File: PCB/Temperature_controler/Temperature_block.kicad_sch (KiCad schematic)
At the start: 16 parts, among them J1 PT IN, J2 Thermocouple IN, SW1 SW_DIP_x05, U2 MAX31865xAP, U3 MAX31856

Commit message: PCB progress
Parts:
- removed SW1: SW_DIP_x05, symbol Switch:SW_DIP_x05
- added C36, C37, C40, C41, C42, C43: 100nF, Capacitor_SMD:C_0805_2012Metric_Pad1.18x1.45mm_HandSolder, symbol Device:C
- added C38, C39: 10nF, Capacitor_SMD:C_0805_2012Metric_Pad1.18x1.45mm_HandSolder, symbol Device:C
- added J11, J12, J13, J15: Conn_01x02_Socket, Connector_Wire:SolderWire-1sqmm_1x02_P5.4mm_D1.4mm_OD2.7mm, symbol Connector:Conn_01x02_Socket
- added J4: T2 IN, TerminalBlock_Phoenix:TerminalBlock_Phoenix_MKDS-1,5-2_1x02_P5.00mm_Horizontal, symbol Connector:Screw_Terminal_01x02
- added J5: RTD2 IN, TerminalBlock_Phoenix:TerminalBlock_Phoenix_MKDS-1,5-4_1x04_P5.00mm_Horizontal, symbol Connector:Screw_Terminal_01x04
- added Q1, Q2, Q3, Q4: BS170F, Package_TO_SOT_SMD:SOT-23, symbol Transistor_FET:BS170F
- added R17, R18: 100Ω, Resistor_SMD:R_0805_2012Metric_Pad1.20x1.40mm_HandSolder, symbol Device:R
- added R19: 400Ω, Resistor_SMD:R_0805_2012Metric_Pad1.20x1.40mm_HandSolder, symbol Device:R
- added R25, R26, R27, R28: 10kΩ, Resistor_SMD:R_0805_2012Metric_Pad1.20x1.40mm_HandSolder, symbol Device:R
- added SW1, SW4: SW_DIP_x04, Button_Switch_SMD:SW_DIP_SPSTx04_Slide_Omron_A6H-4101_W6.15mm_P1.27mm, symbol Switch:SW_DIP_x04
- added U6: MAX31856, Package_SO:TSSOP-14_4.4x5mm_P0.65mm, symbol Sensor_Temperature:MAX31856
- added U7: MAX31865xAP, Package_SO:SSOP-20_5.3x7.2mm_P0.65mm, symbol Sensor_Temperature:MAX31865xAP
- C13, C14, C15, C16, C17, C18, C19, C20: footprint (none) -> Capacitor_SMD:C_0805_2012Metric_Pad1.18x1.45mm_HandSolder
- J1: value PT IN -> RTD1 IN
- J2: value Thermocouple IN -> T1 IN; footprint (none) -> TerminalBlock_Phoenix:TerminalBlock_Phoenix_MKDS-1,5-2_1x02_P5.00mm_Horizontal
- R1, R2, R3: footprint (none) -> Resistor_SMD:R_0805_2012Metric_Pad1.20x1.40mm_HandSolder
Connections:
- net +3.3V: now also C36.1, C37.1, C41.1, C42.1, U6.5 (AVDD), U6.8 (DVDD), U7.2 (DVDD), U7.3 (VDD)
- net GND: now also C36.2, C37.2, C38.2, C39.1, C41.2, C42.2, Q1.2 (S), Q2.2 (S), Q3.2 (S), Q4.2 (S), R25.2, R26.2, R27.2, R28.2, SW1.6, SW4.6, U6.1 (AGND), U6.14 (DGND), U7.13 (GND), U7.18 (DGND), U7.19 (GND)
- net SPI1_CLK: now also U6.10 (SCK), U7.15 (SCLK)
- net SPI1_MISO: now also U6.11 (SDO), U7.17 (SDO)
- net SPI1_MOSI: now also U6.12 (SDI), U7.14 (SDI)
- net at U2.9 (FORCE2): now also SW4.2, SW4.3
- net FORCE+ renamed RTD1_FORCE+
- net RTD1_FORCE+: now also SW4.1, SW4.7
- net FORCE- renamed RTD1_FORCE-
- net RTD1_FORCE-: now also SW4.4
- net MAX31856_CS renamed TC1_CS
- net MAX31856_DRDY renamed TC1_DRDY
- net MAX31856_FAULT renamed TC1_FAULT
- net MAX31865_CS renamed RTD1_CS
- net MAX31865_DRDY renamed RTD1_DRDY
- net RTDIN+ renamed RTD1_RTDIN+
- net RTD1_RTDIN+: now also SW4.8
- net RTDIN- renamed RTD1_RTDIN-
- net RTD1_RTDIN-: now also SW4.5
- net T+ renamed T1+
- net T- renamed T1-
- new net: R19.1, U7.6 (REFIN-), U7.7 (ISENSOR)
- new net: R19.2, U7.4 (BIAS), U7.5 (REFIN+)
- new net: C39.2, C40.1, R17.2, U6.3 (T-)
- new net: C38.1, C40.2, R18.1, U6.4 (T+)
- new net: J15.1 (Pin_1), Q1.3 (D)
- new net: SW1.2, SW1.3, U7.9 (FORCE2)
- new net: J13.1 (Pin_1), Q4.3 (D)
- new net: J12.1 (Pin_1), Q3.3 (D)
- new net: J11.1 (Pin_1), Q2.3 (D)
- new net +24V: J11.2 (Pin_2), J12.2 (Pin_2), J13.2 (Pin_2), J15.2 (Pin_2)
- new net RTD2_CS: U7.16 (~{CS})
- new net RTD2_DRDY: U7.1 (~{DRDY})
- new net RTD2_FORCE+: J5.1 (Pin_1), SW1.1, SW1.7, U7.8 (FORCE+)
- new net RTD2_FORCE-: J5.2 (Pin_2), SW1.4, U7.12 (FORCE-)
- new net RTD2_RTDIN+: C43.2, J5.3 (Pin_3), SW1.8, U7.10 (RTDIN+)
- new net RTD2_RTDIN-: C43.1, J5.4 (Pin_4), SW1.5, U7.11 (RTDIN-)
- new net SSR1: Q1.1 (G), R25.1
- new net SSR2: Q2.1 (G), R26.1
- new net SSR3: Q3.1 (G), R27.1
- new net SSR4: Q4.1 (G), R28.1
- new net T2+: J4.2 (Pin_2), R18.2
- new net T2-: J4.1 (Pin_1), R17.1, U6.2 (BIAS)
- new net TC2_CS: U6.9 (~{CS})
- new net TC2_DRDY: U6.7 (~{DRDY})
- new net TC2_FAULT: U6.13 (~{FAULT})
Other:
- note added: "SSR1 Control"
- note added: "SSR2 Control"
- note added: "SSR3 Control"
- note added: "SSR4 Control"
- moved on the sheet: C13, C14, C15, C16, C17, C18, C19, C20, J1, J2, R1, R2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

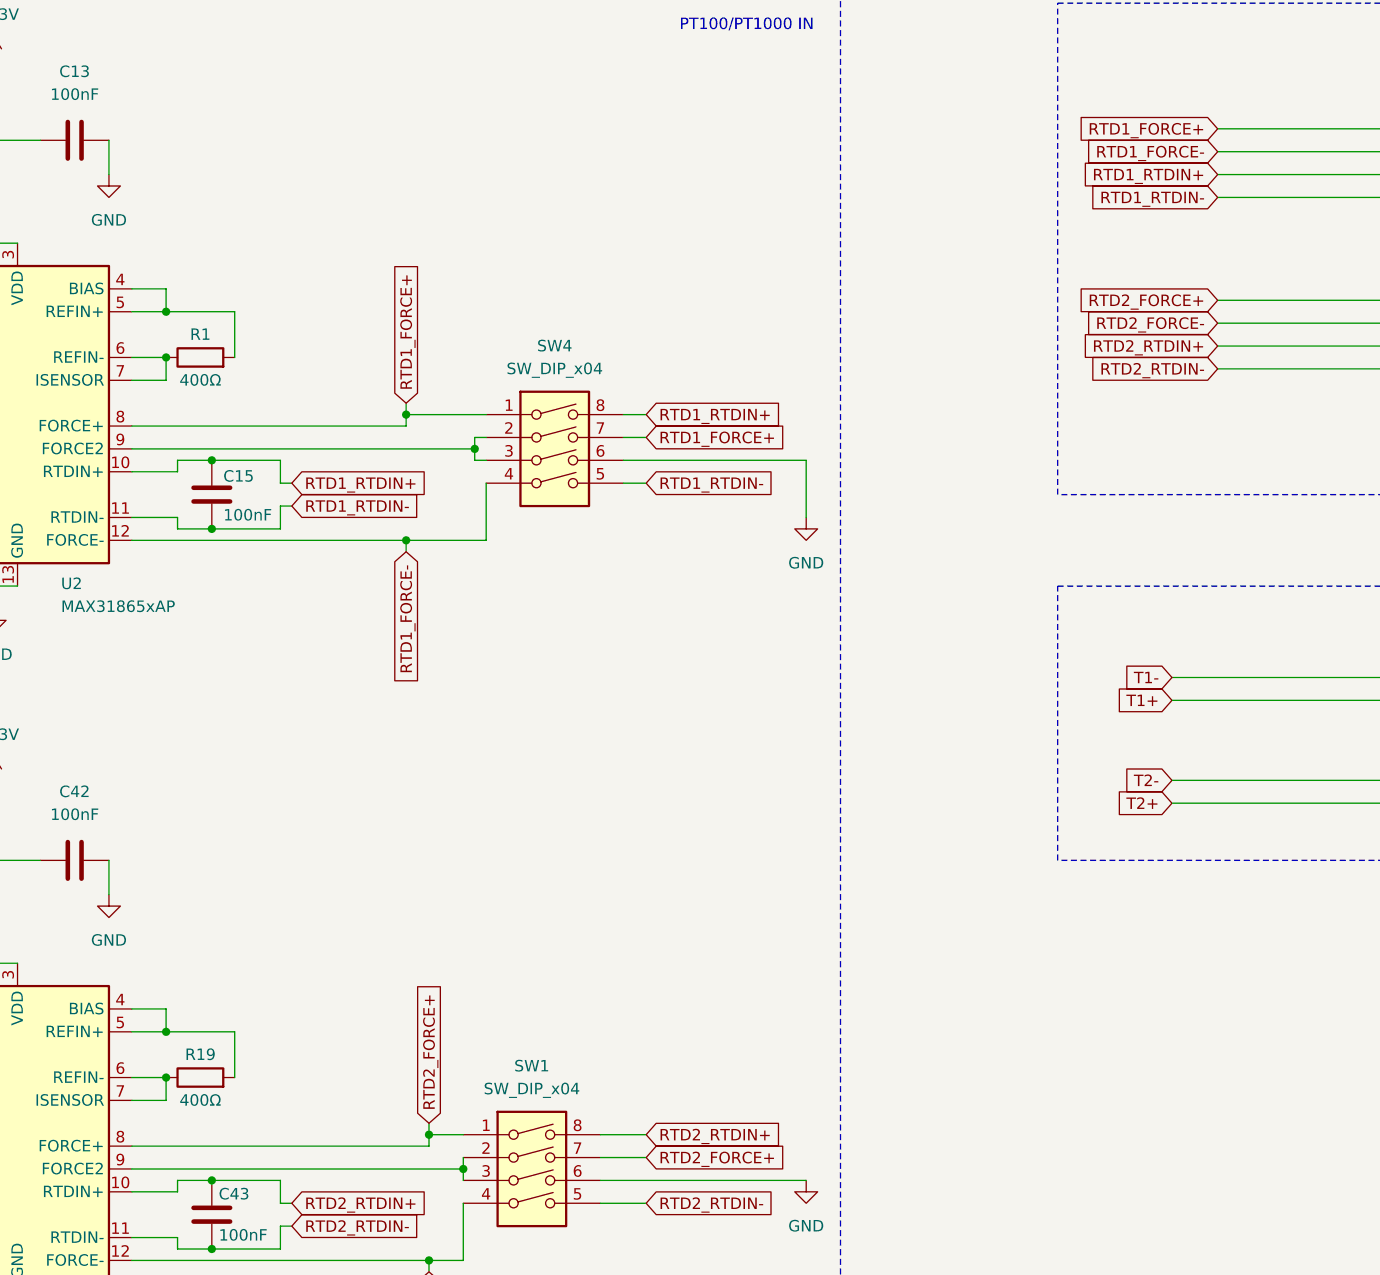
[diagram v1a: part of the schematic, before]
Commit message: Schematic update, PCB progress
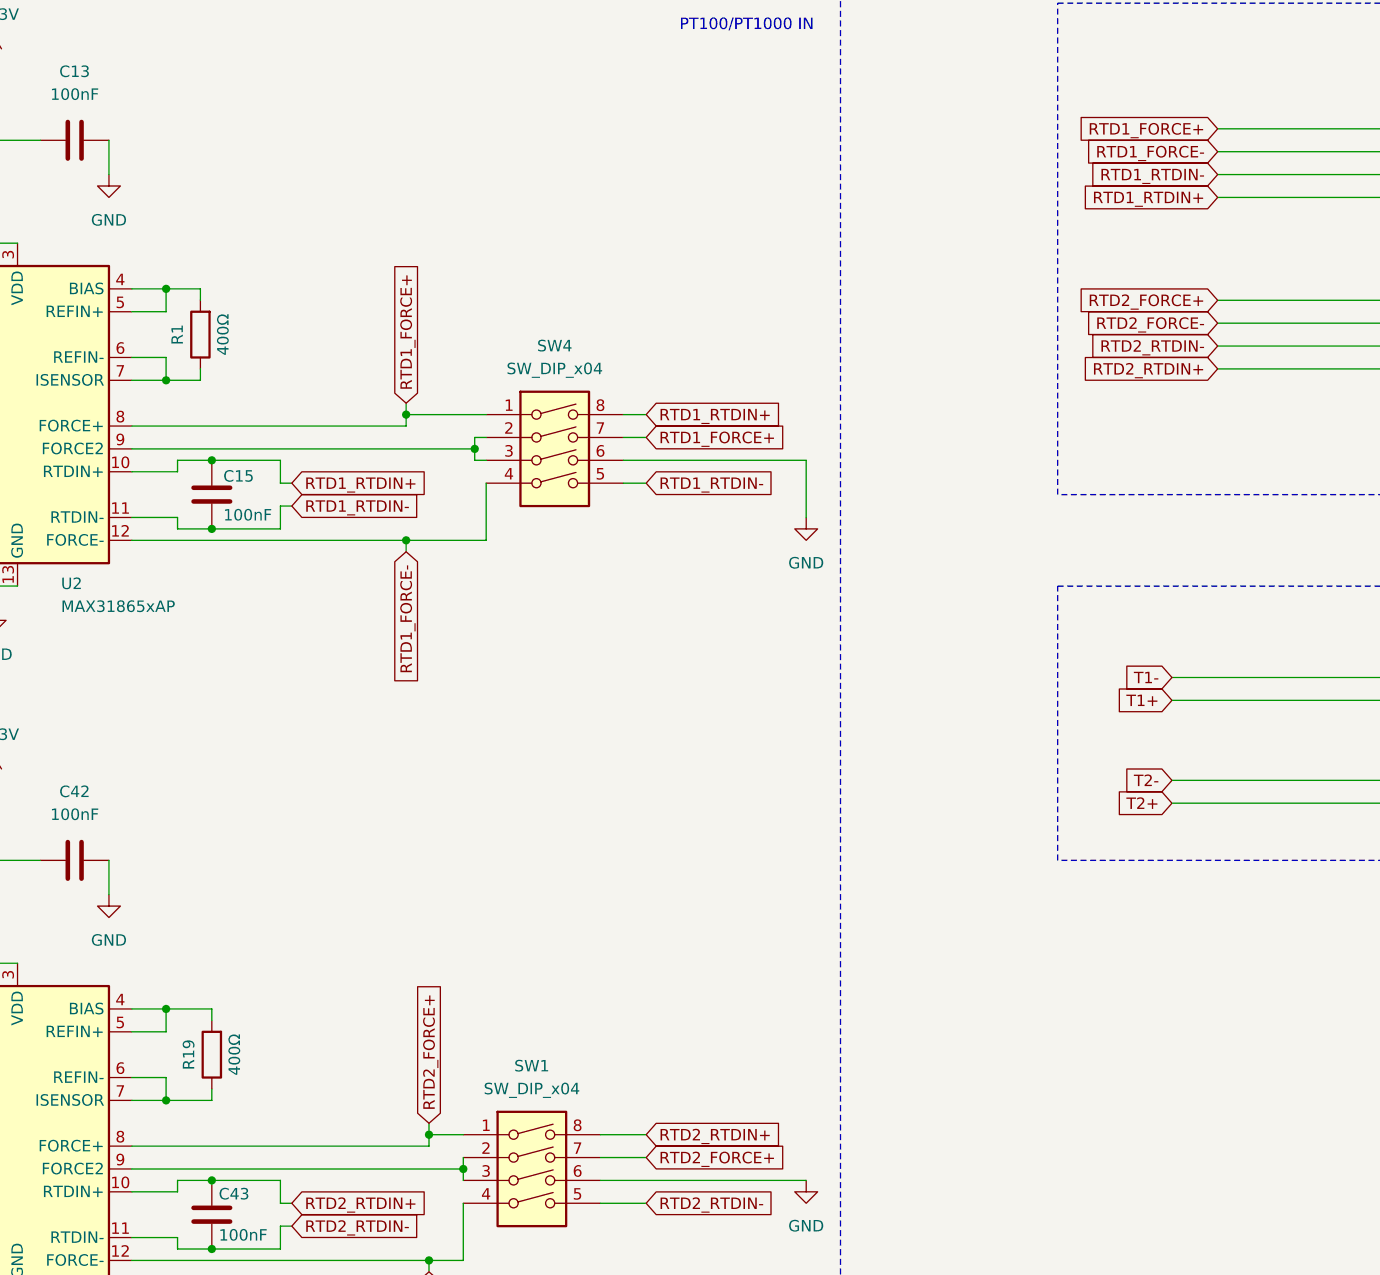
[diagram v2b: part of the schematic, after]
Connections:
- net RTD1_RTDIN+: now also J1.4 (Pin_4); no longer J1.3 (Pin_3)
- net RTD1_RTDIN-: now also J1.3 (Pin_3); no longer J1.4 (Pin_4)
- net RTD2_RTDIN+: now also J5.4 (Pin_4); no longer J5.3 (Pin_3)
- net RTD2_RTDIN-: now also J5.3 (Pin_3); no longer J5.4 (Pin_4)
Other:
- moved on the sheet: R1, R19
